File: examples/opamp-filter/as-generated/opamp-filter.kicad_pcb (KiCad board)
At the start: 2 copper layers, 58 x 42 mm, 22 parts, among them J1 IN, J2 5V, J3 OUT, U1 MCP6001R, U2 MCP6001R

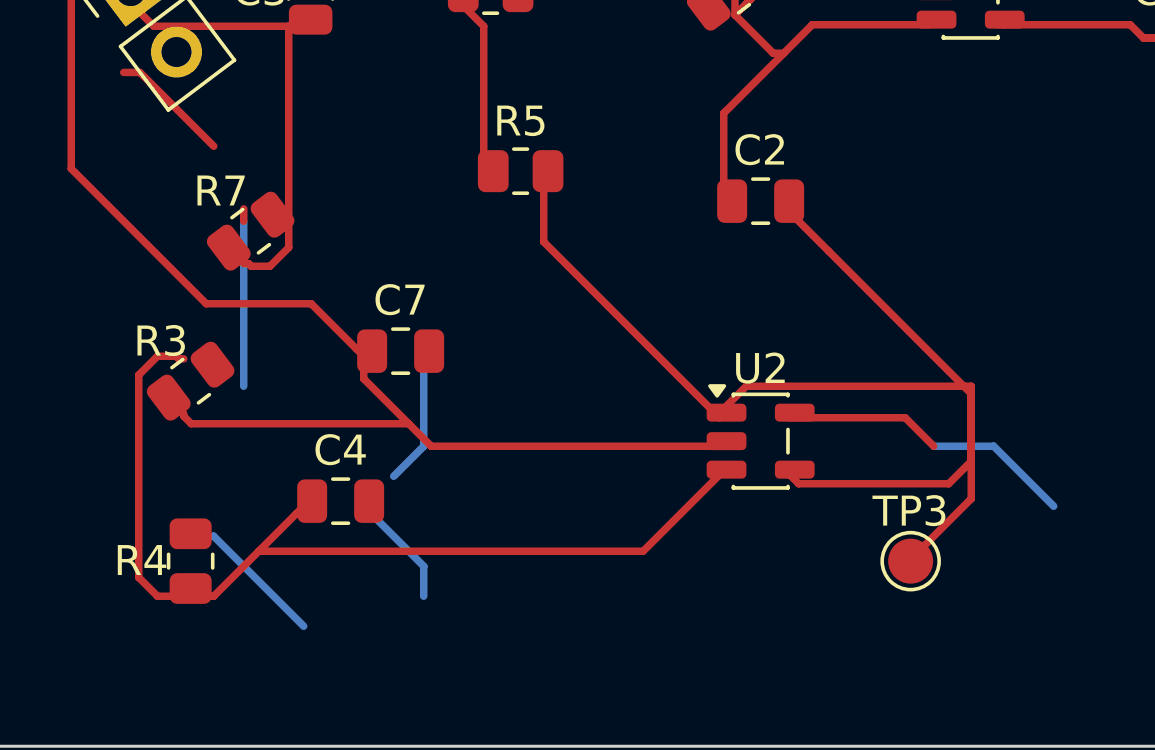
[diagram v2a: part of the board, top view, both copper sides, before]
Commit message: Regenerate the four fast boards without rides or width steps
Zero doubled runs and zero mid-run width changes across all four, by
measurement; all four pass their gates. VREF's whole run at 0.3 mm trips
track.thin_power, and the waiver answers it: the net is a buffered
half-rail loaded in microamps, the rule reads names and cannot read
currents, and the alternative was the width step the reviewer circled.

Co-Authored-By: Claude Fable 5 <noreply@anthropic.com>
Claude-Session: https://claude.ai/code/session_01DUj7Ltu92tWg159mCSacwY
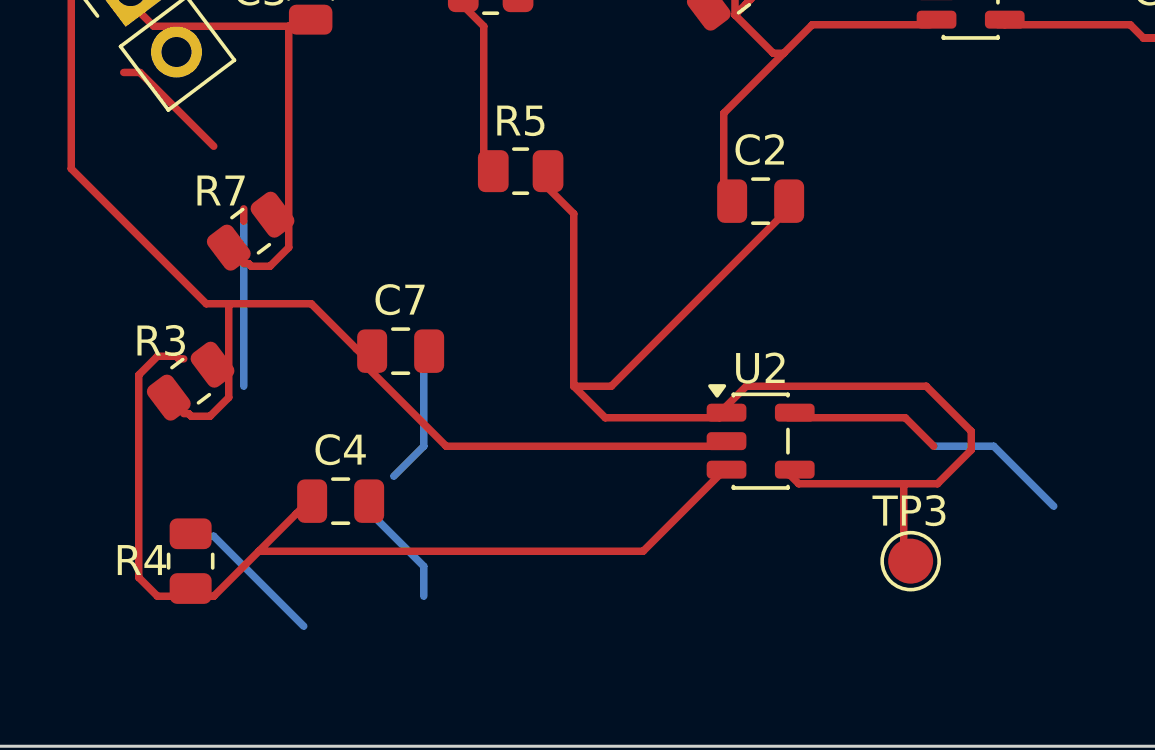
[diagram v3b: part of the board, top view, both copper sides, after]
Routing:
- net +5V: track 84.3 -> 81.2 mm
- net /VREF: track 44.1 -> 42.0 mm
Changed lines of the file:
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@@
 	(segment (start 134.3675 77.95) (end 138.55 77.95) (width 0.25) (layer "F.Cu") (net 7))
 	(segment (start 138.55 77.95) (end 139.0 78.4) (width 0.25) (layer "F.Cu") (net 7))
-	(segment (start 133.0 90.0) (end 125.75 90.0) (width 0.25) (layer "F.Cu") (net 9))
+	(segment (start 131.0 93.25) (end 132.125 93.25) (width 0.25) (layer "F.Cu") (net 9))
+	(segment (start 132.125 93.25) (end 133.25 92.125) (width 0.25) (layer "F.Cu") (net 9))
+	(segment (start 133.25 92.125) (end 133.25 91.5) (width 0.25) (layer "F.Cu") (net 9))
+	(segment (start 133.25 91.5) (end 131.75 90.0) (width 0.25) (layer "F.Cu") (net 9))
+	(segment (start 131.75 90.0) (end 125.75 90.0) (width 0.25) (layer "F.Cu") (net 9))
 	(segment (start 125.75 90.0) (end 125.0 90.75) (width 0.25) (layer "F.Cu") (net 9))
 	(segment (start 125.0 90.75) (end 125.0 90.88) (width 0.25) (layer "F.Cu") (net 9))
 	(segment (start 125.0 90.88) (end 125.0 90.9125) (width 0.25) (layer "F.Cu") (net 9))
 	(segment (start 125.0 90.9125) (end 124.8625 91.05) (width 0.25) (layer "F.Cu") (net 9))
-	(segment (start 124.8625 91.05) (end 119.0 85.1875) (width 0.25) (layer "F.Cu") (net 9))
-	(segment (start 119.0 85.1875) (end 119.0 83.25) (width 0.25) (layer "F.Cu") (net 9))
-	(segment (start 119.0 83.25) (end 119.0 83.0875) (width 0.25) (layer "F.Cu") (net 9))
-	(segment (start 119.0 83.0875) (end 118.9425 83.03) (width 0.25) (layer "F.Cu") (net 9))
-	(segment (start 118.9425 83.03) (end 118.9125 83.0) (width 0.25) (layer "F.Cu") (net 9))
-	(segment (start 124.8625 92.0) (end 115.25 92.0) (width 0.25) (layer "F.Cu") (net 2))
-	(segment (start 115.25 92.0) (end 114.5 91.25) (width 0.25) (layer "F.Cu") (net 2))
+	(segment (start 124.8625 91.05) (end 121.05 91.05) (width 0.25) (layer "F.Cu") (net 9))
+	(segment (start 121.05 91.05) (end 120.0 90.0) (width 0.25) (layer "F.Cu") (net 9))
+	(segment (start 124.8625 92.0) (end 115.75 92.0) (width 0.25) (layer "F.Cu") (net 2))
+	(segment (start 115.75 92.0) (end 113.0 89.25) (width 0.25) (layer "F.Cu") (net 2))
+	(segment (start 113.0 89.25) (end 113.0 89.05) (width 0.25) (layer "F.Cu") (net 2))
+	(segment (start 113.0 89.05) (end 113.025 89.025) (width 0.25) (layer "F.Cu") (net 2))
+	(segment (start 113.025 89.025) (end 113.0 89.0) (width 0.25) (layer "F.Cu") (net 2))
+	(segment (start 113.0 89.0) (end 112.75 88.75) (width 0.25) (layer "F.Cu") (net 2))
+	(segment (start 112.75 88.75) (end 111.25 87.25) (width 0.25) (layer "F.Cu") (net 2))
+	(segment (start 111.25 87.25) (end 108.5 87.25) (width 0.25) (layer "F.Cu") (net 2))
 	(segment (start 124.8625 92.95) (end 122.3125 95.5) (width 0.25) (layer "F.Cu") (net 6))
 	(segment (start 122.3125 95.5) (end 109.5 95.5) (width 0.25) (layer "F.Cu") (net 6))
@@
 	(segment (start 125.375 73.375) (end 125.375 77.625) (width 0.25) (layer "F.Cu") (net 3))
 	(segment (start 144.0 72.0) (end 141.75 74.25) (width 0.25) (layer "F.Cu") (net 7))
-	(segment (start 131.0 96.0) (end 131.2 95.8) (width 0.25) (layer "F.Cu") (net 9))
-	(segment (start 131.2 95.8) (end 133.25 93.75) (width 0.25) (layer "F.Cu") (net 9))
-	(segment (start 133.25 93.75) (end 133.25 90.25) (width 0.25) (layer "F.Cu") (net 9))
-	(segment (start 133.25 90.25) (end 133.0 90.0) (width 0.25) (layer "F.Cu") (net 9))
-	(segment (start 133.0 90.0) (end 128.5 85.5) (width 0.25) (layer "F.Cu") (net 9))
-	(segment (start 128.5 85.5) (end 127.25 84.25) (width 0.25) (layer "F.Cu") (net 9))
-	(segment (start 127.25 84.25) (end 127.2 84.25) (width 0.25) (layer "F.Cu") (net 9))
-	(segment (start 127.2 84.25) (end 126.98 84.03) (width 0.25) (layer "F.Cu") (net 9))
-	(segment (start 126.98 84.03) (end 126.95 84.0) (width 0.25) (layer "F.Cu") (net 9))
+	(segment (start 131.0 96.0) (end 131.0 95.83) (width 0.25) (layer "F.Cu") (net 9))
+	(segment (start 131.0 95.83) (end 131.0 93.25) (width 0.25) (layer "F.Cu") (net 9))
 	(segment (start 125.05 84.0) (end 125.05 83.83) (width 0.25) (layer "F.Cu") (net 3))
 	(segment (start 125.05 83.83) (end 125.05 83.8) (width 0.25) (layer "F.Cu") (net 3))
@@
 	(segment (start 127.1375 92.95) (end 127.2 92.95) (width 0.25) (layer "F.Cu") (net 9))
 	(segment (start 127.2 92.95) (end 127.5 93.25) (width 0.25) (layer "F.Cu") (net 9))
-	(segment (start 127.5 93.25) (end 132.5 93.25) (width 0.25) (layer "F.Cu") (net 9))
-	(segment (start 132.5 93.25) (end 133.25 92.5) (width 0.25) (layer "F.Cu") (net 9))
-	(segment (start 133.25 92.5) (end 133.25 90.0) (width 0.25) (layer "F.Cu") (net 9))
-	(segment (start 133.25 90.0) (end 133.0 90.0) (width 0.25) (layer "F.Cu") (net 9))
+	(segment (start 127.5 93.25) (end 131.0 93.25) (width 0.25) (layer "F.Cu") (net 9))
+	(segment (start 120.0 90.0) (end 121.25 90.0) (width 0.25) (layer "F.Cu") (net 9))
+	(segment (start 121.25 90.0) (end 127.0 84.25) (width 0.25) (layer "F.Cu") (net 9))
+	(segment (start 127.0 84.25) (end 127.0 84.05) (width 0.25) (layer "F.Cu") (net 9))
+	(segment (start 127.0 84.05) (end 126.98 84.03) (width 0.25) (layer "F.Cu") (net 9))
+	(segment (start 126.98 84.03) (end 126.95 84.0) (width 0.25) (layer "F.Cu") (net 9))
+	(segment (start 120.0 90.0) (end 120.0 84.25) (width 0.25) (layer "F.Cu") (net 9))
+	(segment (start 120.0 84.25) (end 119.0 83.25) (width 0.25) (layer "F.Cu") (net 9))
+	(segment (start 119.0 83.25) (end 119.0 83.0875) (width 0.25) (layer "F.Cu") (net 9))
+	(segment (start 119.0 83.0875) (end 118.9425 83.03) (width 0.25) (layer "F.Cu") (net 9))
+	(segment (start 118.9425 83.03) (end 118.9125 83.0) (width 0.25) (layer "F.Cu") (net 9))
 	(segment (start 107.0 89.0875) (end 106.8375 89.0875) (width 0.25) (layer "F.Cu") (net 6))
 	(segment (start 106.8375 89.0875) (end 106.75 89.0) (width 0.25) (layer "F.Cu") (net 6))
@@
 	(segment (start 103.25 72.75) (end 103.25 82.75) (width 0.25) (layer "F.Cu") (net 2))
 	(segment (start 103.25 82.75) (end 107.75 87.25) (width 0.25) (layer "F.Cu") (net 2))
-	(segment (start 107.75 87.25) (end 111.25 87.25) (width 0.25) (layer "F.Cu") (net 2))
-	(segment (start 111.25 87.25) (end 112.75 88.75) (width 0.25) (layer "F.Cu") (net 2))
-	(segment (start 112.75 88.75) (end 113.0 89.0) (width 0.25) (layer "F.Cu") (net 2))
-	(segment (start 113.0 89.0) (end 113.025 89.025) (width 0.25) (layer "F.Cu") (net 2))
-	(segment (start 113.025 89.025) (end 113.0 89.05) (width 0.25) (layer "F.Cu") (net 2))
-	(segment (start 113.0 89.05) (end 113.0 89.25) (width 0.25) (layer "F.Cu") (net 2))
-	(segment (start 113.0 89.25) (end 113.0 89.75) (width 0.25) (layer "F.Cu") (net 2))
-	(segment (start 113.0 89.75) (end 114.5 91.25) (width 0.25) (layer "F.Cu") (net 2))
+	(segment (start 107.75 87.25) (end 108.5 87.25) (width 0.25) (layer "F.Cu") (net 2))
 	(segment (start 127.5 76.25) (end 127.5 73.0) (width 0.25) (layer "B.Cu") (net 2))
-	(segment (start 107.0 90.9125) (end 107.0 91.0) (width 0.25) (layer "F.Cu") (net 2))
-	(segment (start 107.0 91.0) (end 107.25 91.25) (width 0.25) (layer "F.Cu") (net 2))
-	(segment (start 107.25 91.25) (end 114.5 91.25) (width 0.25) (layer "F.Cu") (net 2))
+	(segment (start 107.0 90.9125) (end 107.1625 90.9125) (width 0.25) (layer "F.Cu") (net 2))
+	(segment (start 107.1625 90.9125) (end 107.25 91.0) (width 0.25) (layer "F.Cu") (net 2))
+	(segment (start 107.25 91.0) (end 107.875 91.0) (width 0.25) (layer "F.Cu") (net 2))
+	(segment (start 107.875 91.0) (end 108.5 90.375) (width 0.25) (layer "F.Cu") (net 2))
+	(segment (start 108.5 90.375) (end 108.5 87.25) (width 0.25) (layer "F.Cu") (net 2))
 )

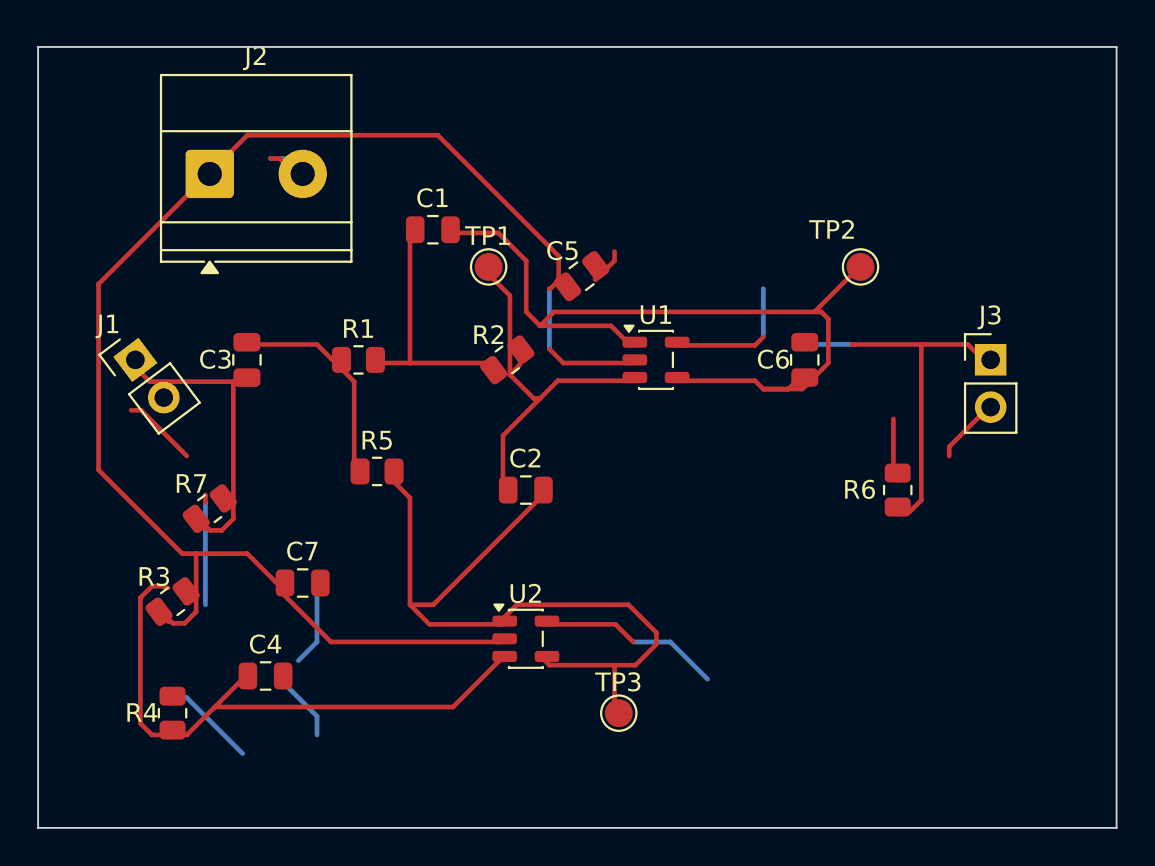
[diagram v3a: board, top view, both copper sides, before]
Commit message: Keep vias out of the lands they would drain
The reviewer's next one, and it is not one board's problem: vias were
landing inside surface-mount lands across the set. A hole in a land is a
hole solder wicks down during reflow - the joint above it starves, and
nothing on the assembled board tells that apart from a cold one.
Via-in-pad is a real technique and a filled-and-capped process, not a
drawing; a layout that has not specified the process may not draw it.

The router was the source. `_blocked` skips a route's own net, so
nothing stopped a layer change from happening on the very land the route
started at, and eighteen vias across three boards sat in one. Pads are
now marked as pads in the obstacle list and every one of them, whoever
owns it, is a cell where a via may not go - so an escape that has to
reach the plane leaves the land first and turns its via beside it. The
stitching pass kept ground vias a via-radius from ground lands where it
kept signal ones a radius plus clearance; both are the same distance
now, because the plane gains nothing from touching a land it can reach a
stub away.

`via.in_pad` measures the copper gap from every via to every land and
reports what is left. The exposed thermal pad under a package is exempt
- the via array in one is the datasheet's own answer, and nothing a
signal reaches is four square millimetres. It blocks under the
ai-generated policy: a generated board has no reason to draw this.

The test fixture had one too, a via twenty-five microns into C1's ground
land; it moves three tenths of a millimetre and the board is DRC clean
on both matrix versions as before.

Co-Authored-By: Claude Fable 5 <noreply@anthropic.com>
Claude-Session: https://claude.ai/code/session_01DUj7Ltu92tWg159mCSacwY
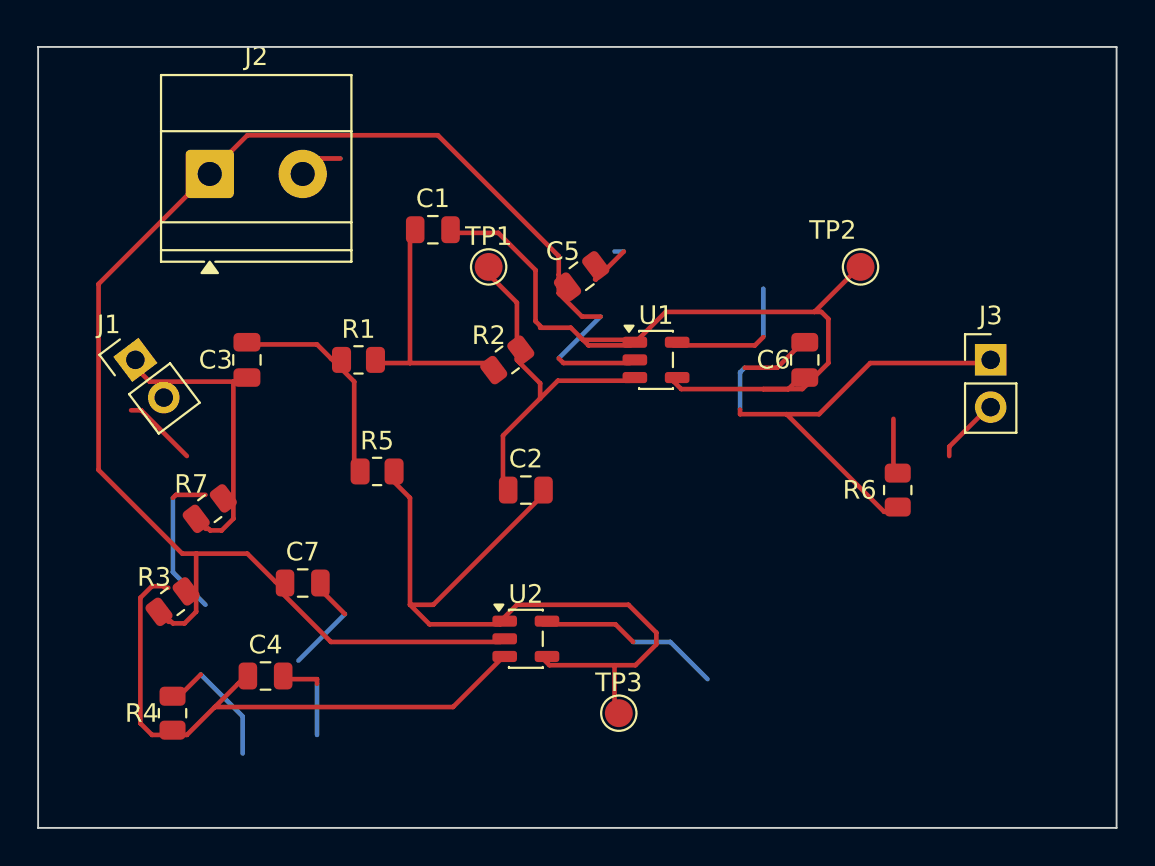
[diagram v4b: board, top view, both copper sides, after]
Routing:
- net GND: track 53.0 -> 62.3 mm
- net /OUT_AC: track 20.6 -> 28.5 mm
- net +5V: track 81.2 -> 83.2 mm
- net /OUT: track 46.9 -> 44.9 mm
- net /FILT_IN: track 20.4 -> 19.3 mm
